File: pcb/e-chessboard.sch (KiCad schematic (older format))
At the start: 66 parts, among them J1 POWER, J2 UART, Q1 BC847, Q2 BC847, SW1 Reset, SW2 Boot, U1 ESP32-WROOM-32U, U10 MAGNET_LDR, U11 MAGNET_LDR, U12 MAGNET_LDR, U13 NCV7608, U2 AOZ1280, U3 NCV7608, U4 MAGNET_LDR, U5 MAGNET_LDR, U6 MAGNET_LDR, U7 MAGNET_LDR, U8 MAGNET_LDR, U9 MAGNET_LDR

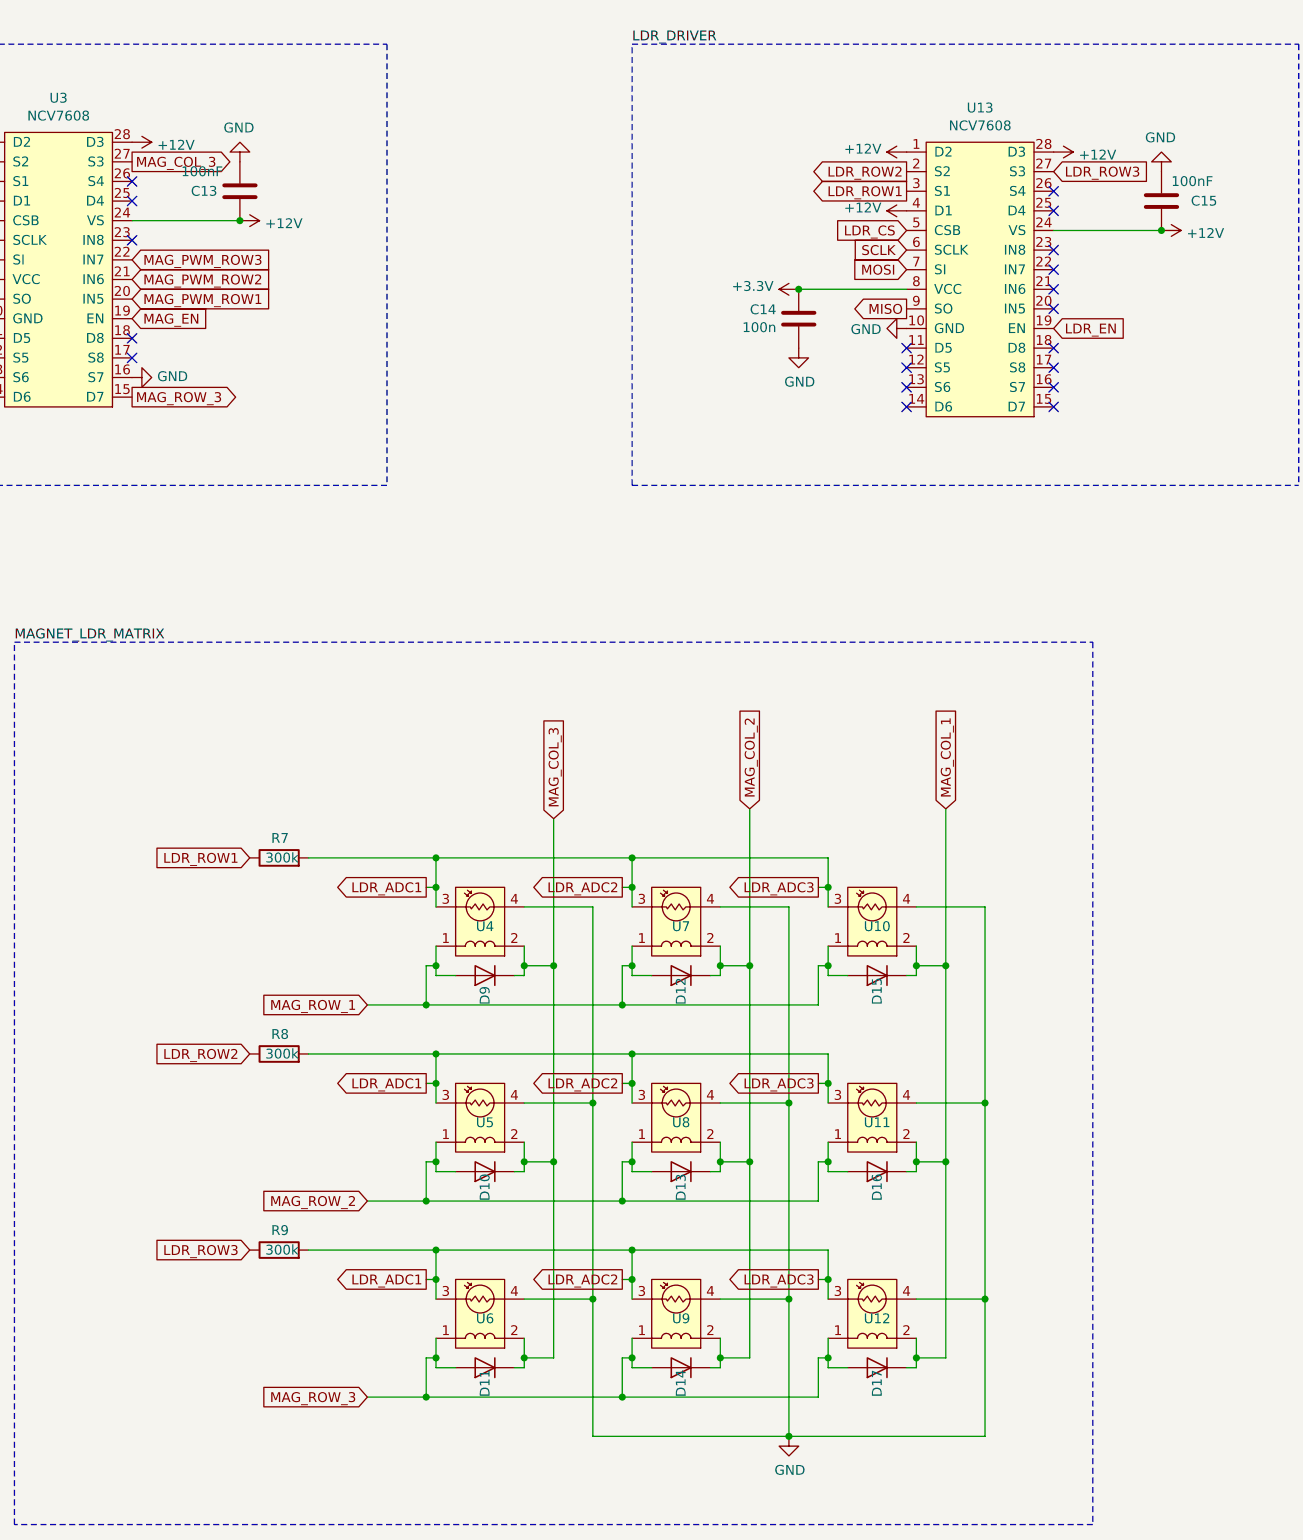
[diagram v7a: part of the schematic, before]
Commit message: fix(kicad): fixing ldr issue
Still not 100% sure weather this is working.
Tried to fix #2.
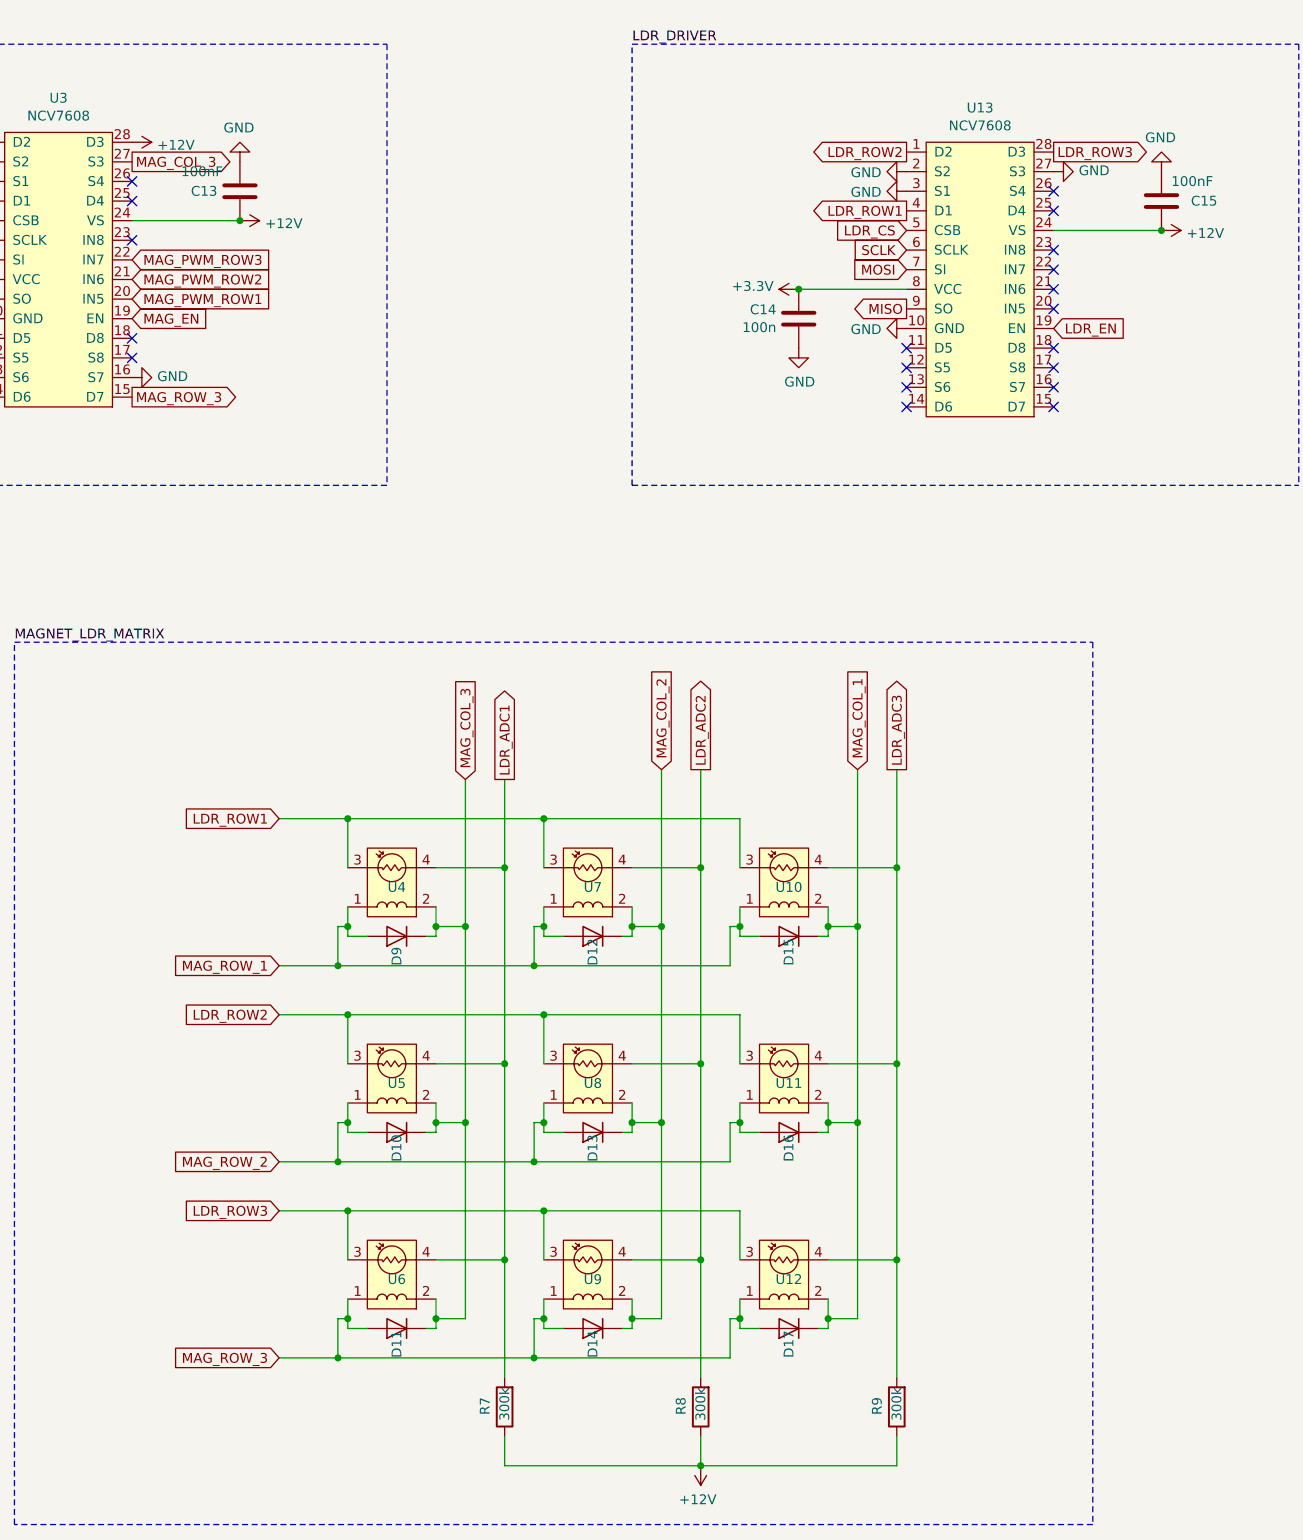
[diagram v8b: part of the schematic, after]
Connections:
- net +12V: now also R7.1, R8.1, R9.1; no longer U13.1 (D2), U13.28 (D3), U13.4 (D1)
- net GND: now also U13.2 (S2), U13.27 (S3), U13.3 (S1); no longer U10.4, U11.4, U12.4, U4.4, U5.4, U6.4, U7.4, U8.4, U9.4
- net LDR_ADC1: now also U4.4, U5.4, U6.4; no longer D4.2 (A), D5.1 (K), D6.2 (A), D7.1 (K), R8.2, R9.2, U1.6 (IO34), U1.7 (IO35), U10.3, U11.3, U12.3, U4.3, U5.3, U6.3, U7.3, U8.3, U9.3
- net LDR_ROW1: now also U10.3, U13.4 (D1), U4.3, U7.3; no longer R7.1, U13.3 (S1)
- net LDR_ROW2: now also U11.3, U13.1 (D2), U5.3, U8.3; no longer R8.1, U13.2 (S2)
- net LDR_ROW3: now also U12.3, U13.28 (D3), U6.3, U9.3; no longer R9.1, U13.27 (S3)
- new net LDR_ADC2: D6.2 (A), D7.1 (K), R8.2, U1.6 (IO34), U7.4, U8.4, U9.4
- new net LDR_ADC3: D4.2 (A), D5.1 (K), R9.2, U1.7 (IO35), U10.4, U11.4, U12.4
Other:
- moved on the sheet: D10, D11, D12, D13, D14, D15, D16, D17, D9, R7, R8, R9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
